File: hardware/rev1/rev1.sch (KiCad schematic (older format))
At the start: 42 parts, among them J1 Conn_01x09_Female, J2 RFM9X_header, J3 Conn_01x03_Male, U1 BNO055, U2 MPL3115A2, U3 Teensy3.6, U4 BMI088, U5 ADXL345BCCZ, Y1 Crystal_32kHz768

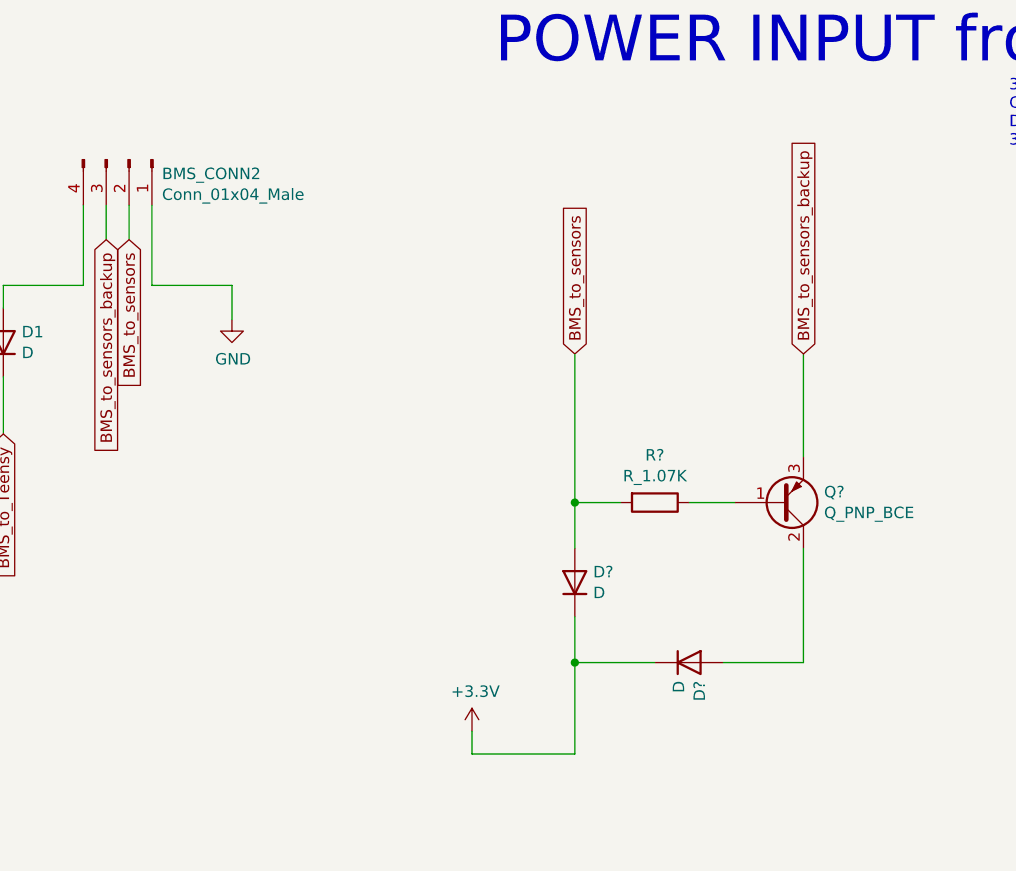
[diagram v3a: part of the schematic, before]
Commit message: add transistor footprint and datasheet
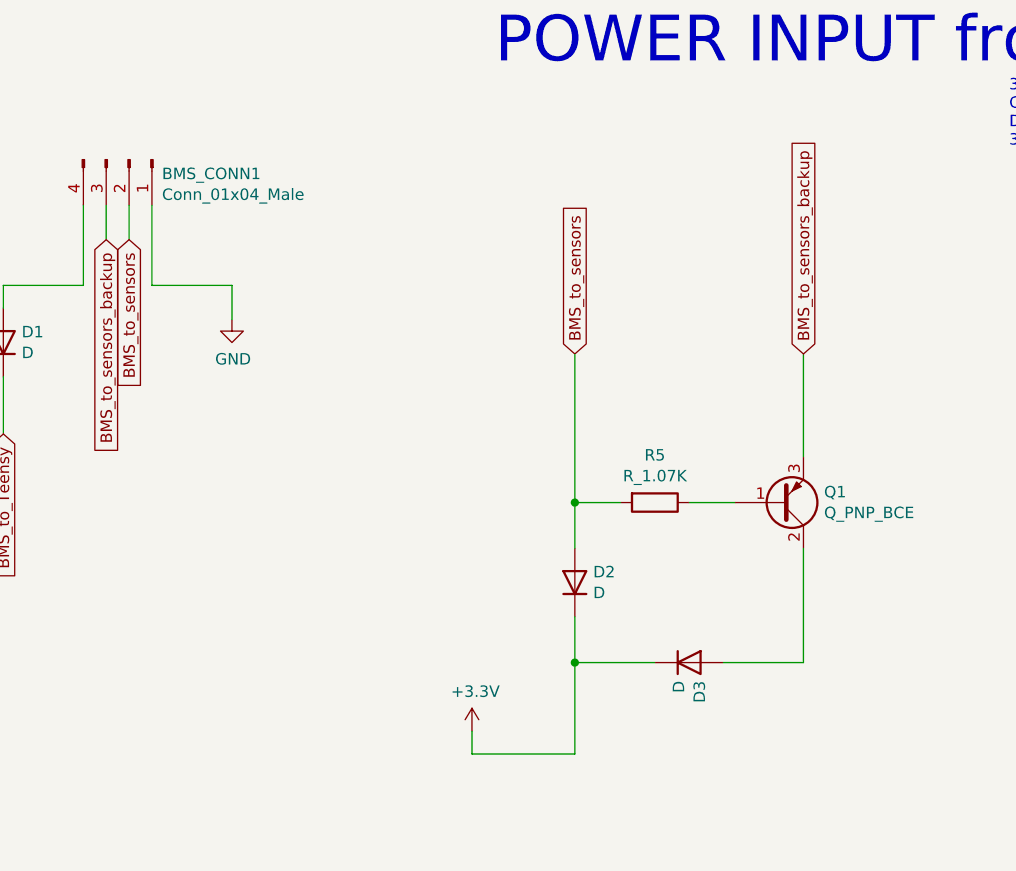
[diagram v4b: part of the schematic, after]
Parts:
- Q1: renamed from Q?; footprint (none) -> Package_TO_SOT_THT:TO-220-3_Horizontal_TabDown
- gave numbers to parts that had none: 3
- renumbered BMS_CONN2 to BMS_CONN1
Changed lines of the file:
@@
 TX\n\nRX
 $Comp
-L Connector:Conn_01x04_Male BMS_CONN2
+L Connector:Conn_01x04_Male BMS_CONN1
 U 1 1 602BDAB1
 P 25200 10650
-F 0 "BMS_CONN2" V 25262 10794 50  0000 L CNN
+F 0 "BMS_CONN1" V 25262 10794 50  0000 L CNN
 F 1 "Conn_01x04_Male" V 25353 10794 50  0000 L CNN
 F 2 "Connector_PinHeader_2.54mm:PinHeader_1x04_P2.54mm_Vertical" H 25200 10650 50  0001 C CNN
@@
 $EndComp
 $Comp
-L power:GND #PWR?
+L power:GND #PWR04
 U 1 1 602C00BA
 P 25650 11350
-F 0 "#PWR?" H 25650 11100 50  0001 C CNN
+F 0 "#PWR04" H 25650 11100 50  0001 C CNN
 F 1 "GND" H 25655 11177 50  0000 C CNN
 F 2 "" H 25650 11350 50  0001 C CNN
@@
 	25650 11350 25650 11200
 $Comp
-L Device:Q_PNP_BCE Q?
+L Device:Q_PNP_BCE Q1
 U 1 1 60396DCD
 P 28050 12150
-F 0 "Q?" H 28240 12104 50  0000 L CNN
+F 0 "Q1" H 28240 12104 50  0000 L CNN
 F 1 "Q_PNP_BCE" H 28240 12195 50  0000 L CNN
-F 2 "" H 28250 12250 50  0001 C CNN
+F 2 "Package_TO_SOT_THT:TO-220-3_Horizontal_TabDown" H 28250 12250 50  0001 C CNN
 F 3 "~" H 28050 12150 50  0001 C CNN
 	1    28050 12150
@@
 $EndComp
 $Comp
-L Device:D D?
+L Device:D D2
 U 1 1 60398902
 P 27150 12500
-F 0 "D?" V 27196 12420 50  0000 R CNN
+F 0 "D2" V 27196 12420 50  0000 R CNN
 F 1 "D" V 27105 12420 50  0000 R CNN
 F 2 "footprints:D_0805_OEM" H 27150 12500 50  0001 C CNN
@@
 	28150 11500 28150 11950
 $Comp
-L preferred_parts:R_1.07K R?
+L preferred_parts:R_1.07K R5
 U 1 1 603A35C2
 P 27500 12150
-F 0 "R?" V 27293 12150 50  0000 C CNN
+F 0 "R5" V 27293 12150 50  0000 C CNN
 F 1 "R_1.07K" V 27384 12150 50  0000 C CNN
 F 2 "footprints:R_0805_OEM" H 27430 12150 50  0001 C CNN
@@
 	26700 13250 26700 13150
 $Comp
-L power:+3.3V #PWR?
+L power:+3.3V #PWR014
 U 1 1 603D4A0D
 P 26700 13150
-F 0 "#PWR?" H 26700 13000 50  0001 C CNN
+F 0 "#PWR014" H 26700 13000 50  0001 C CNN
 F 1 "+3.3V" H 26715 13323 50  0000 C CNN
 F 2 "" H 26700 13150 50  0001 C CNN
@@
 BMS_to_sensors_backup
 $Comp
-L Device:D D?
+L Device:D D3
 U 1 1 603EDD6A
 P 27650 12850
-F 0 "D?" V 27696 12770 50  0000 R CNN
+F 0 "D3" V 27696 12770 50  0000 R CNN
 F 1 "D" V 27605 12770 50  0000 R CNN
 F 2 "footprints:D_0805_OEM" H 27650 12850 50  0001 C CNN
@@
 	3300 8400 4200 8400
 $Comp
-L power:+3.3V #PWR?
+L power:+3.3V #PWR03
 U 1 1 6045910E
 P 3500 2350
-F 0 "#PWR?" H 3500 2200 50  0001 C CNN
+F 0 "#PWR03" H 3500 2200 50  0001 C CNN
 F 1 "+3.3V" H 3515 2523 50  0000 C CNN
 F 2 "" H 3500 2350 50  0001 C CNN

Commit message: wip
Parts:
- added BMS_CONN2: Conn_01x04_Male, Connector_PinHeader_2.54mm:PinHeader_1x04_P2.54mm_Vertical, symbol Connector:Conn_01x04_Male
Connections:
- net BMS_to_sensors: now also BMS_CONN2.2 (Pin_2)
- net BMS_to_sensors_backup: now also BMS_CONN2.3 (Pin_3)
- net GND: now also BMS_CONN2.1 (Pin_1)
- net at BMS_CONN1.4 (Pin_4), D1.2 (A): now also BMS_CONN2.4 (Pin_4)
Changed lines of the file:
@@
 3.3V_TEENSY
 NoConn ~ 29450 11150
-$Comp
-L Device:D D1
-U 1 1 60275618
-P 24650 11450
-F 0 "D1" V 24696 11370 50  0000 R CNN
-F 1 "D" V 24605 11370 50  0000 R CNN
-F 2 "footprints:D_0805_OEM" H 24650 11450 50  0001 C CNN
-F 3 "~" H 24650 11450 50  0001 C CNN
-	1    24650 11450
-	0    -1   -1   0
-$EndComp
-Text Notes 23000 12100 0    50   ~ 0
-power can only flow into the Teensy,\nnot out of the 5V pin
 NoConn ~ 17800 15400
 Wire Wire Line
@@
 Text Notes 28500 5850 0    50   ~ 0
 TX\n\nRX
-$Comp
-L Connector:Conn_01x04_Male BMS_CONN1
-U 1 1 602BDAB1
-P 25200 10650
-F 0 "BMS_CONN1" V 25262 10794 50  0000 L CNN
-F 1 "Conn_01x04_Male" V 25353 10794 50  0000 L CNN
-F 2 "Connector_PinHeader_2.54mm:PinHeader_1x04_P2.54mm_Vertical" H 25200 10650 50  0001 C CNN
-F 3 "~" H 25200 10650 50  0001 C CNN
-	1    25200 10650
-	0    1    1    0
-$EndComp
-$Comp
-L power:GND #PWR04
-U 1 1 602C00BA
-P 25650 11350
-F 0 "#PWR04" H 25650 11100 50  0001 C CNN
-F 1 "GND" H 25655 11177 50  0000 C CNN
-F 2 "" H 25650 11350 50  0001 C CNN
-F 3 "" H 25650 11350 50  0001 C CNN
-	1    25650 11350
-	1    0    0    -1
-$EndComp
-Text GLabel 24650 11850 3    50   Input ~ 0
-BMS_to_Teensy
-Wire Wire Line
-	25200 10850 25200 11000
-Wire Wire Line
-	25100 10850 25100 11000
-Text GLabel 25100 11000 3    50   Input ~ 0
-BMS_to_sensors_backup
-Text GLabel 25200 11000 3    50   Input ~ 0
-BMS_to_sensors
 Text Notes 25800 5800 0    50   ~ 0
 (GPS) RX -> TX (Teensy)\n(GPS) TX -> RX (Teensy)\n
@@
 Text GLabel 29700 6300 2    50   Input ~ 0
 BMS_to_Teensy
-Wire Wire Line
-	24650 11850 24650 11600
-Wire Wire Line
-	25000 11200 24650 11200
-Wire Wire Line
-	24650 11200 24650 11300
-Wire Wire Line
-	25000 10850 25000 11200
-Wire Wire Line
-	25300 10850 25300 11200
-Wire Wire Line
-	25300 11200 25650 11200
-Wire Wire Line
-	25650 11350 25650 11200
 $Comp
 L Device:Q_PNP_BCE Q1
@@
 	1    0    0    -1
 $EndComp
+Wire Wire Line
+	25650 11350 25650 11200
+Wire Wire Line
+	25300 11200 25650 11200
+Wire Wire Line
+	25300 10850 25300 11200
+Wire Wire Line
+	25000 10850 25000 11200
+Wire Wire Line
+	24650 11200 24650 11300
+Wire Wire Line
+	25000 11200 24650 11200
+Wire Wire Line
+	24650 11850 24650 11600
+Text GLabel 25200 11000 3    50   Input ~ 0
+BMS_to_sensors
+Text GLabel 25100 11000 3    50   Input ~ 0
+BMS_to_sensors_backup
+Wire Wire Line
+	25100 10850 25100 11000
+Wire Wire Line
+	25200 10850 25200 11000
+Text GLabel 24650 11850 3    50   Input ~ 0
+BMS_to_Teensy
+$Comp
+L power:GND #PWR04
+U 1 1 602C00BA
+P 25650 11350
+F 0 "#PWR04" H 25650 11100 50  0001 C CNN
+F 1 "GND" H 25655 11177 50  0000 C CNN
+F 2 "" H 25650 11350 50  0001 C CNN
+F 3 "" H 25650 11350 50  0001 C CNN
+	1    25650 11350
+	1    0    0    -1
+$EndComp
+$Comp
+L Connector:Conn_01x04_Male BMS_CONN1
+U 1 1 602BDAB1
+P 25200 10650
+F 0 "BMS_CONN1" V 25262 10794 50  0000 L CNN
+F 1 "Conn_01x04_Male" V 25353 10794 50  0000 L CNN
+F 2 "Connector_PinHeader_2.54mm:PinHeader_1x04_P2.54mm_Vertical" H 25200 10650 50  0001 C CNN
+F 3 "~" H 25200 10650 50  0001 C CNN
+	1    25200 10650
+	0    1    1    0
+$EndComp
+Text Notes 23000 12100 0    50   ~ 0
+power can only flow into the Teensy,\nnot out of the 5V pin
+$Comp
+L Device:D D1
+U 1 1 60275618
+P 24650 11450
+F 0 "D1" V 24696 11370 50  0000 R CNN
+F 1 "D" V 24605 11370 50  0000 R CNN
+F 2 "footprints:D_0805_OEM" H 24650 11450 50  0001 C CNN
+F 3 "~" H 24650 11450 50  0001 C CNN
+	1    24650 11450
+	0    -1   -1   0
+$EndComp
+Wire Wire Line
+	22450 11350 22450 11200
+Wire Wire Line
+	22100 11200 22450 11200
+Wire Wire Line
+	22100 10850 22100 11200
+Wire Wire Line
+	21800 10850 21800 11200
+Wire Wire Line
+	21800 11200 21450 11200
+Text GLabel 22000 11000 3    50   Input ~ 0
+BMS_to_sensors
+Text GLabel 21900 11000 3    50   Input ~ 0
+BMS_to_sensors_backup
+Wire Wire Line
+	21900 10850 21900 11000
+Wire Wire Line
+	22000 10850 22000 11000
+$Comp
+L power:GND #PWR015
+U 1 1 6047CFA5
+P 22450 11350
+F 0 "#PWR015" H 22450 11100 50  0001 C CNN
+F 1 "GND" H 22455 11177 50  0000 C CNN
+F 2 "" H 22450 11350 50  0001 C CNN
+F 3 "" H 22450 11350 50  0001 C CNN
+	1    22450 11350
+	1    0    0    -1
+$EndComp
+$Comp
+L Connector:Conn_01x04_Male BMS_CONN2
+U 1 1 6047CFAF
+P 22000 10650
+F 0 "BMS_CONN2" V 22062 10794 50  0000 L CNN
+F 1 "Conn_01x04_Male" V 22153 10794 50  0000 L CNN
+F 2 "Connector_PinHeader_2.54mm:PinHeader_1x04_P2.54mm_Vertical" H 22000 10650 50  0001 C CNN
+F 3 "~" H 22000 10650 50  0001 C CNN
+	1    22000 10650
+	0    1    1    0
+$EndComp
+Text Notes 19800 12100 0    50   ~ 0
+power can only flow into the Teensy,\nnot out of the 5V pin
+Wire Wire Line
+	21450 12150 22900 12150
+Wire Wire Line
+	22900 12150 22900 11200
+Wire Wire Line
+	22900 11200 24650 11200
+Wire Wire Line
+	21450 11200 21450 12150
+Connection ~ 24650 11200
 $EndSCHEMATC

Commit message: wip
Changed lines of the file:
@@
 	21450 11200 21450 12150
 Connection ~ 24650 11200
+Text GLabel 26550 13250 0    50   Input ~ 0
+3.3VBMS
+Wire Wire Line
+	26700 13250 26550 13250
+Connection ~ 26700 13250
 $EndSCHEMATC

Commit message: rearrange GPS
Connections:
- net ENABLE_GPS: now also U3.33 (36_A17_PWM); no longer U3.32 (35_A16_PWM)
- net FIX: now also U3.32 (35_A16_PWM); no longer U3.35 (38_A19_PWM_SDA1)
- net PPS: now also U3.35 (38_A19_PWM_SDA1); no longer U3.33 (36_A17_PWM)
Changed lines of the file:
@@
 Text GLabel 27400 5800 0    50   Input ~ 0
 TX
-Text GLabel 27400 6200 0    50   Input ~ 0
+Text GLabel 27400 5900 0    50   Input ~ 0
 FIX
-Text GLabel 27400 5900 0    50   Input ~ 0
+Text GLabel 27400 6000 0    50   Input ~ 0
 ENABLE_GPS
 NoConn ~ 29700 3400
@@
 Wire Wire Line
 	13700 16450 13700 16600
-Text GLabel 27400 6000 0    50   Input ~ 0
+Text GLabel 27400 6200 0    50   Input ~ 0
 PPS
 $Comp

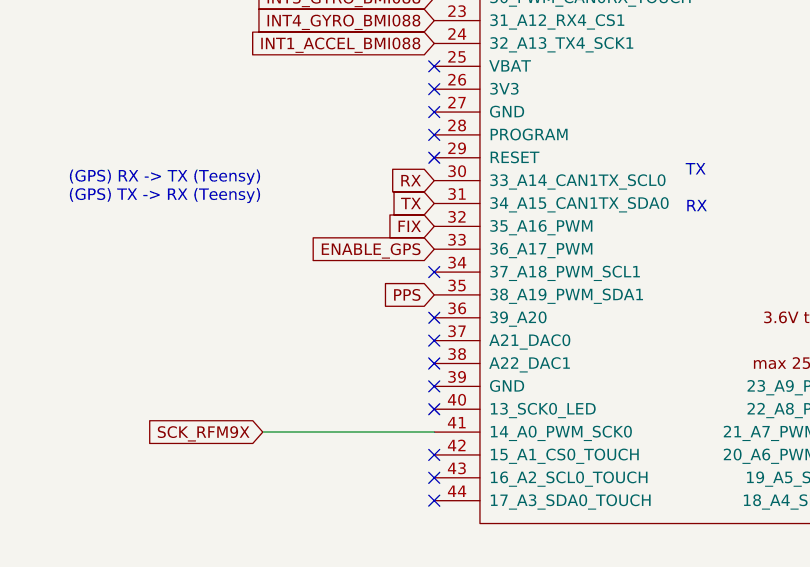
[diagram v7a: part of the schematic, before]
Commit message: switch pins on GPS
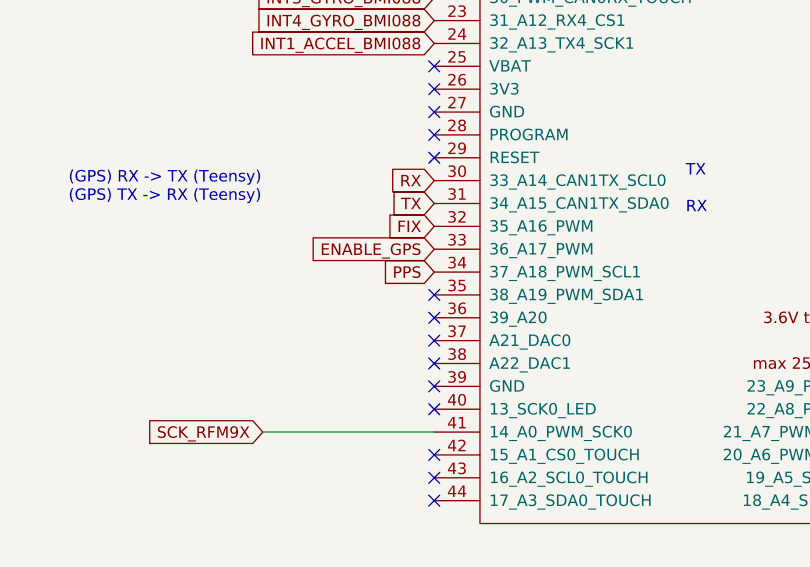
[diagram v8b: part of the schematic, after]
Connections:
- net PPS: now also U3.34 (37_A18_PWM_SCL1); no longer U3.35 (38_A19_PWM_SDA1)
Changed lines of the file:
@@
 	1    0    0    -1
 $EndComp
-NoConn ~ 27400 6100
 $Comp
 L power:+3.3V #PWR08
@@
 Wire Wire Line
 	13700 16450 13700 16600
-Text GLabel 27400 6200 0    50   Input ~ 0
+Text GLabel 27400 6100 0    50   Input ~ 0
 PPS
 $Comp
@@
 	26700 13250 26550 13250
 Connection ~ 26700 13250
+NoConn ~ 27400 6200
 $EndSCHEMATC
